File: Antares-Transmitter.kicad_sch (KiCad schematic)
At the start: 0 parts

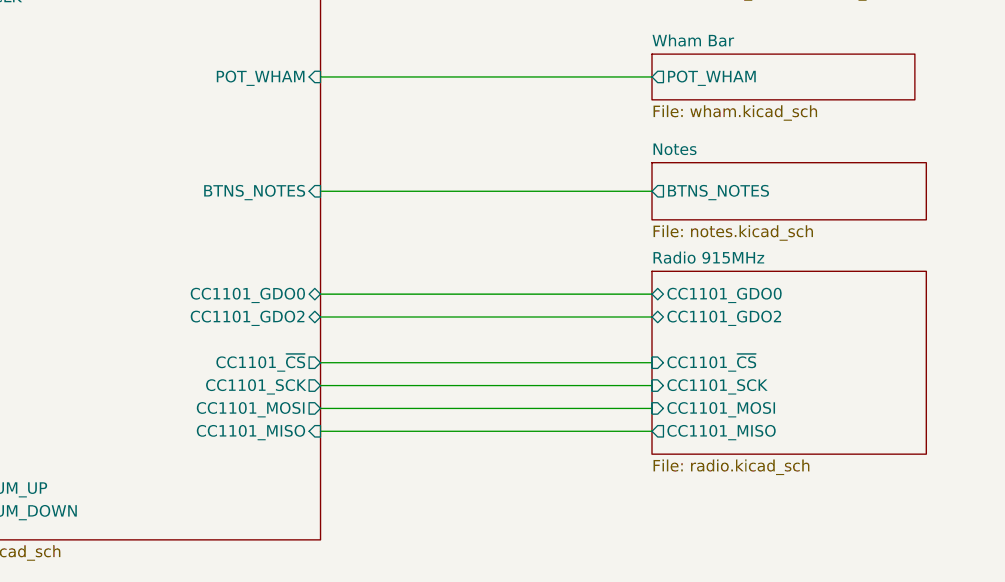
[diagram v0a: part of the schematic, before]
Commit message: t:art: fixed noted reading, using 75hc165 for Input expander
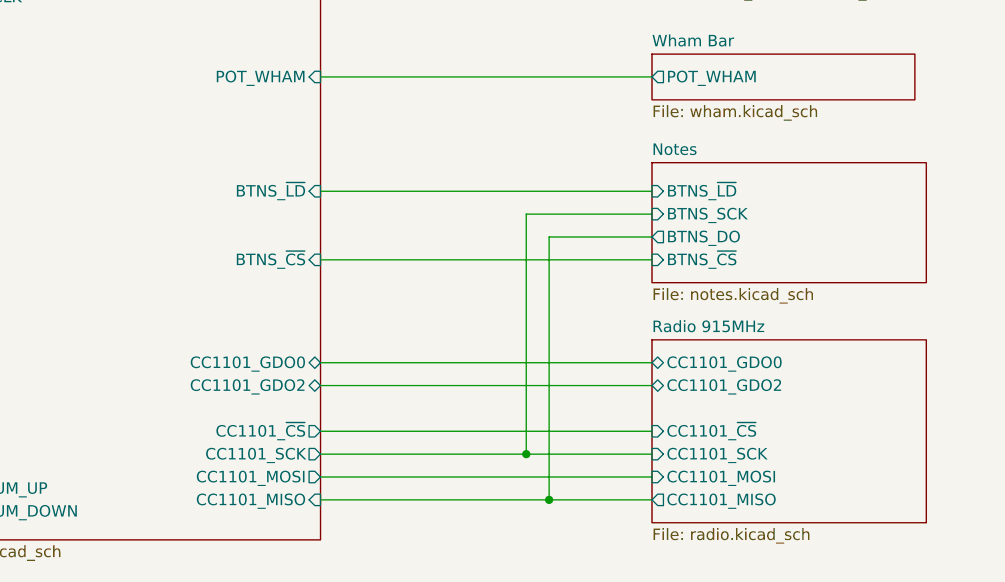
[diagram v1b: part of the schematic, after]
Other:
- sheet MCU ports: added BTNS_~{CS}, BTNS_~{LD}; removed BTNS_NOTES
- sheet Notes ports: added BTNS_DO, BTNS_SCK, BTNS_~{CS}, BTNS_~{LD}; removed BTNS_NOTES
